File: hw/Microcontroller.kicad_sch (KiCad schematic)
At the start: 22 parts, among them SW1 Reset, SW2 Boot0, U3 STM32G431CBT6, Y1 16 MHz

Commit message: huge schematic rework
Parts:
- D1, D2: footprint Resistor_SMD:R_0603_1608Metric -> LED_THT:LED_D5.0mm
- R5, R6: value 470 -> 1k; LCSC C23179 -> C21190
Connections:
- net +3.3V: now also SW2.2; no longer R4.2
- net GND: now also R4.1; no longer SW2.1
- net STM_BOOT0: now also R4.2; no longer R4.1
- net at R3.1: now also SW2.1; no longer SW2.2
- net STM_USART1_RX: no longer names the net of U3.32 (PA10)
- no-connect marks 16 -> 17
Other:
- moved on the sheet: C17, C18, R1, R2, R3, R4, SW1, SW2

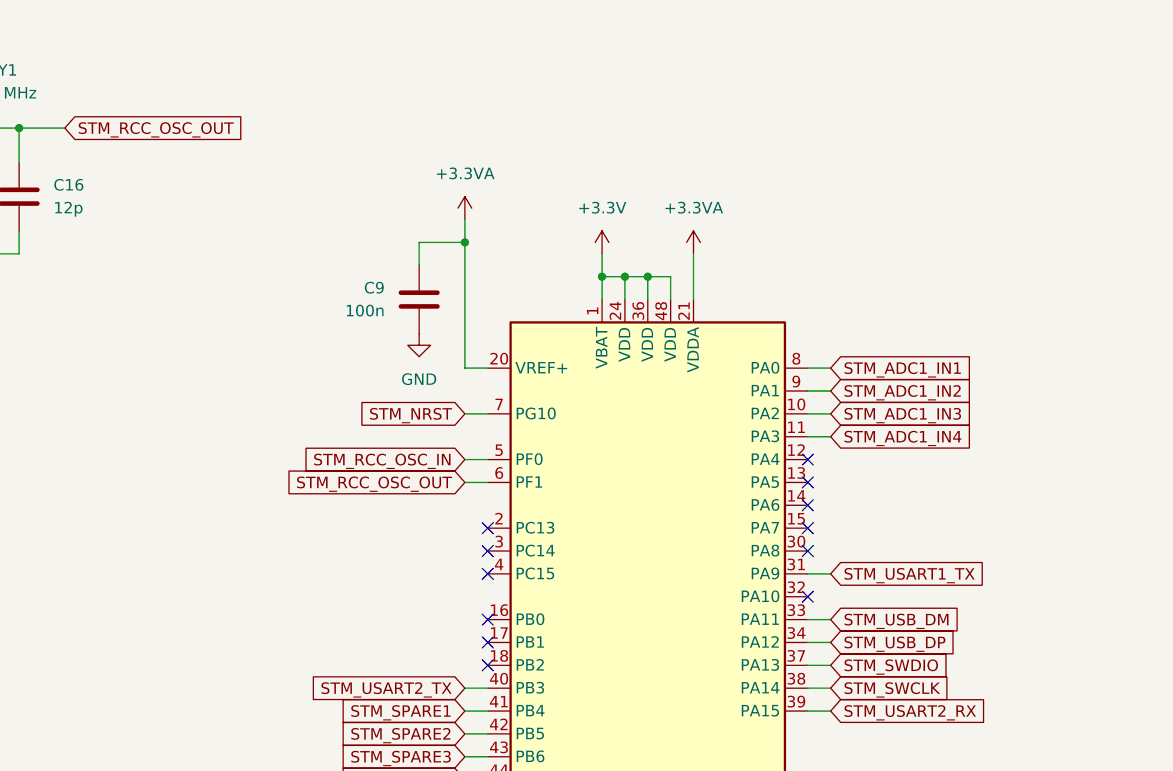
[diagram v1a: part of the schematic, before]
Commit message: added new pcb design, ERC errors not fixed yet
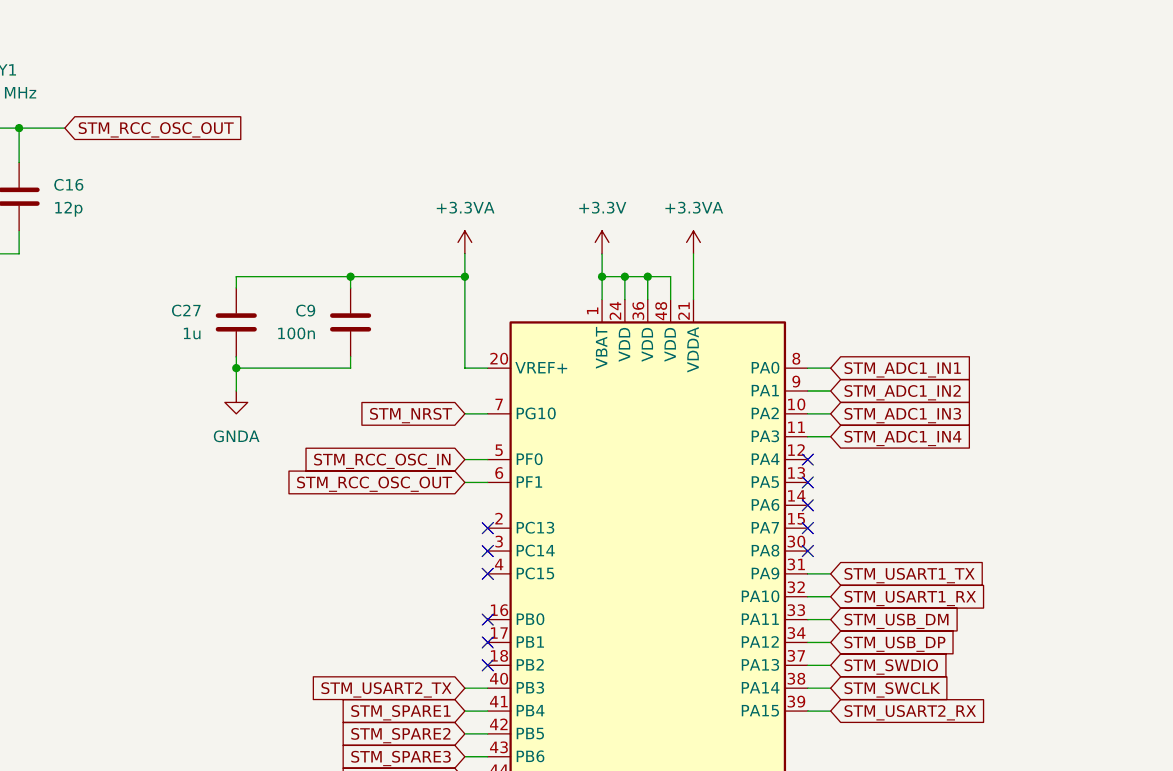
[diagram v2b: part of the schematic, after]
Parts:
- added C27: 1u, Capacitor_SMD:C_0603_1608Metric, symbol Device:C
- D1, D2: footprint LED_THT:LED_D5.0mm -> LED_THT:LED_D3.0mm
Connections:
- net +3.3VA: now also C27.1
- net GND: no longer C9.2
- net GNDA: now also C9.2, C27.2
- net STM_USART1_RX: now reaches U3.32 (PA10)
- no-connect marks 17 -> 16
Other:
- moved on the sheet: C9

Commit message: updates to hardware layer
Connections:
- net STM_ADC2_IN17: now reaches U3.12 (PA4)
- net STM_ADC2_IN13: now reaches U3.13 (PA5)
- net STM_ADC2_IN3: now reaches U3.14 (PA6)
- net STM_ADC2_IN4: now reaches U3.15 (PA7)
- no-connect marks 16 -> 12
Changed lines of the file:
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@@
 	)
 	(no_connect
-		(at 161.29 83.82)
+		(at 125.73 127)
+	)
+	(no_connect
+		(at 125.73 137.16)
+	)
+	(no_connect
+		(at 125.73 134.62)
+	)
+	(no_connect
+		(at 125.73 93.98)
 	)
 	(no_connect
@@
 	)
 	(no_connect
-		(at 125.73 127)
-	)
-	(no_connect
-		(at 125.73 137.16)
-	)
-	(no_connect
-		(at 125.73 134.62)
-	)
-	(no_connect
-		(at 125.73 93.98)
-	)
-	(no_connect
-		(at 161.29 86.36)
-	)
-	(no_connect
 		(at 125.73 88.9)
-	)
-	(no_connect
-		(at 161.29 88.9)
 	)
 	(no_connect
@@
 	)
 	(no_connect
-		(at 161.29 81.28)
-	)
-	(no_connect
 		(at 125.73 101.6)
 	)
@@
 	(wire
 		(pts
+			(xy 161.29 83.82) (xy 163.83 83.82)
+		)
+		(stroke
+			(width 0)
+			(type default)
+		)
+	)
+	(wire
+		(pts
 			(xy 123.19 114.3) (xy 125.73 114.3)
 		)
@@
 	(wire
 		(pts
+			(xy 161.29 81.28) (xy 163.83 81.28)
+		)
+		(stroke
+			(width 0)
+			(type default)
+		)
+	)
+	(wire
+		(pts
 			(xy 43.18 148.59) (xy 43.18 151.13)
 		)
@@
 	(wire
 		(pts
+			(xy 161.29 86.36) (xy 163.83 86.36)
+		)
+		(stroke
+			(width 0)
+			(type default)
+		)
+	)
+	(wire
+		(pts
 			(xy 148.59 147.32) (xy 146.05 147.32)
 		)
@@
 	(wire
 		(pts
+			(xy 161.29 88.9) (xy 163.83 88.9)
+		)
+		(stroke
+			(width 0)
+			(type default)
+		)
+	)
+	(wire
+		(pts
 			(xy 205.74 27.94) (xy 218.44 27.94)
 		)
@@
 		)
 	)
+	(global_label "STM_ADC2_IN17"
+		(shape input)
+		(at 163.83 81.28 0)
+		(fields_autoplaced yes)
+		(effects
+			(font
+				(size 1.27 1.27)
+			)
+			(justify left)
+		)
+		(property "Intersheetrefs" "${INTERSHEET_REFS}"
+			(at 181.5713 81.28 0)
+			(effects
+				(font
+					(size 1.27 1.27)
+				)
+				(justify left)
+				(hide yes)
+			)
+		)
+	)
 	(global_label "STM_SPARE3"
 		(shape input)
@@
 		)
 	)
+	(global_label "STM_ADC2_IN13"
+		(shape input)
+		(at 163.83 83.82 0)
+		(fields_autoplaced yes)
+		(effects
+			(font
+				(size 1.27 1.27)
+			)
+			(justify left)
+		)
+		(property "Intersheetrefs" "${INTERSHEET_REFS}"
+			(at 181.5713 83.82 0)
+			(effects
+				(font
+					(size 1.27 1.27)
+				)
+				(justify left)
+				(hide yes)
+			)
+		)
+	)
 	(global_label "STM_LED2"
 		(shape input)
@@
 		)
 	)
+	(global_label "STM_ADC2_IN3"
+		(shape input)
+		(at 163.83 86.36 0)
+		(fields_autoplaced yes)
+		(effects
+			(font
+				(size 1.27 1.27)
+			)
+			(justify left)
+		)
+		(property "Intersheetrefs" "${INTERSHEET_REFS}"
+			(at 180.3618 86.36 0)
+			(effects
+				(font
+					(size 1.27 1.27)
+				)
+				(justify left)
+				(hide yes)
+			)
+		)
+	)
 	(global_label "STM_SWCLK"
 		(shape input)
@@
 			(effects
 				(font
+					(size 1.27 1.27)
+				)
+				(justify left)
+				(hide yes)
+			)
+		)
+	)
+	(global_label "STM_ADC2_IN4"
+		(shape input)
+		(at 163.83 88.9 0)
+		(fields_autoplaced yes)
+		(effects
+			(font
+				(size 1.27 1.27)
+			)
+			(justify left)
+		)
+		(property "Intersheetrefs" "${INTERSHEET_REFS}"
+			(at 180.3618 88.9 0)
+			(effects
+				(font

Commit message: removed MIDI Thru and updated Connector positioning
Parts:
- D1, D2: footprint LED_THT:LED_D3.0mm -> LED_THT:LED_D5.0mm
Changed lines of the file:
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@@
 			)
 		)
-		(property "Footprint" "LED_THT:LED_D3.0mm"
+		(property "Footprint" "LED_THT:LED_D5.0mm"
 			(at 55.88 154.94 0)
 			(effects
@@
 			)
 		)
-		(property "Footprint" "LED_THT:LED_D3.0mm"
+		(property "Footprint" "LED_THT:LED_D5.0mm"
 			(at 43.18 154.94 0)
 			(effects

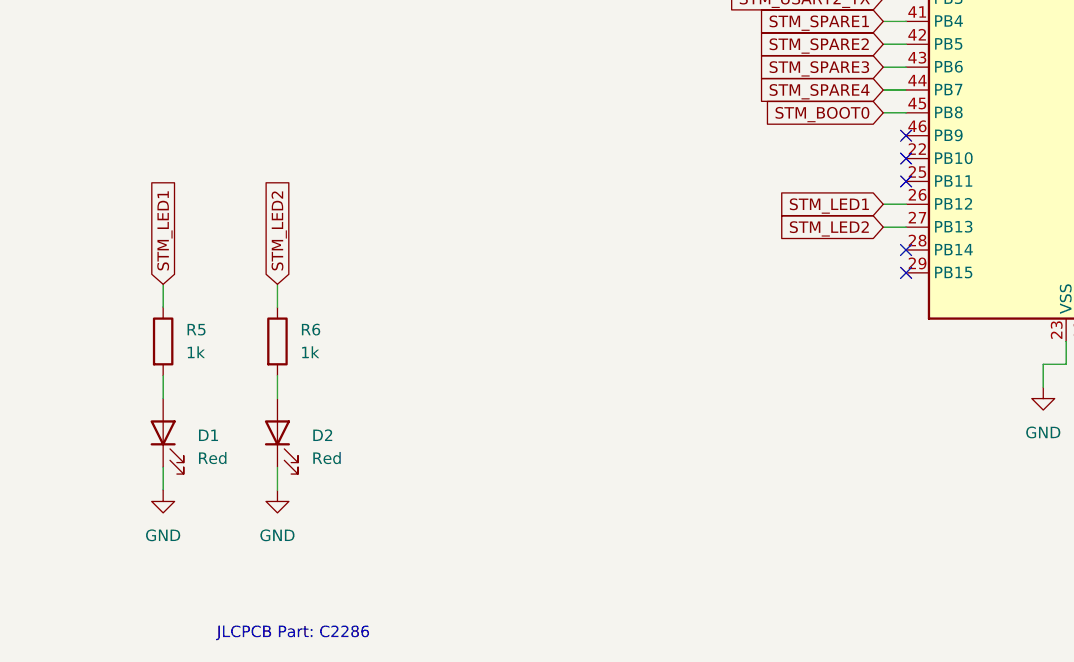
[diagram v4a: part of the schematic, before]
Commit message: updated connector positions and added new RGB led
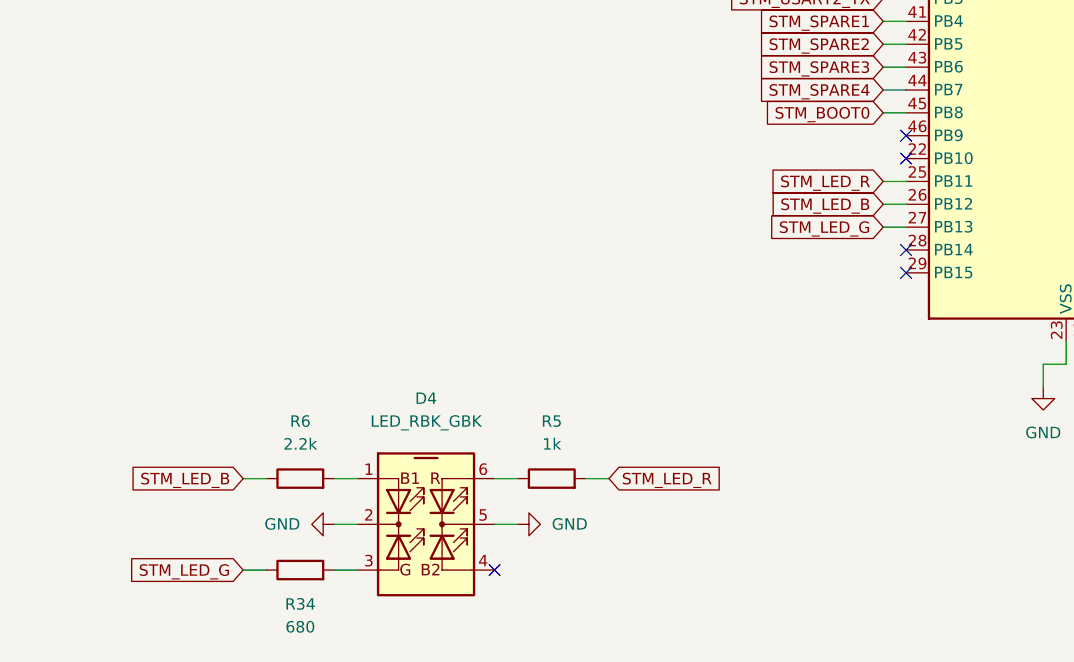
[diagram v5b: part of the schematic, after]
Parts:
- removed D1, D2: Red, LED_THT:LED_D5.0mm, symbol Device:LED
- added D4: LED_RBK_GBK, LED_THT_6Pin:LED_D5.0mm_6Pin, symbol Midi_Expressor:LED_RBK_GBK
- added R34: 680, Resistor_SMD:R_0603_1608Metric, symbol Device:R
- R6: value 1k -> 2.2k; LCSC C21190 -> (none)
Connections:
- net GND: now also D4.2 (K1), D4.5 (K2)
- net at R6.2: now also D4.1 (B1A)
- net STM_LED_R: now reaches U3.25 (PB11)
- net STM_LED_R: now also R5.2
- net STM_LED1: no longer names the net of R5.1
- net STM_LED1: now also D4.6 (RA); no longer U3.26 (PB12)
- net STM_LED2 renamed STM_LED_B
- net STM_LED_B: now also U3.26 (PB12); no longer U3.27 (PB13)
- new net: D4.3 (GA), R34.2
- new net STM_LED_G: R34.1, U3.27 (PB13)
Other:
- note removed: "JLCPCB Part: C2286"
- moved on the sheet: R5

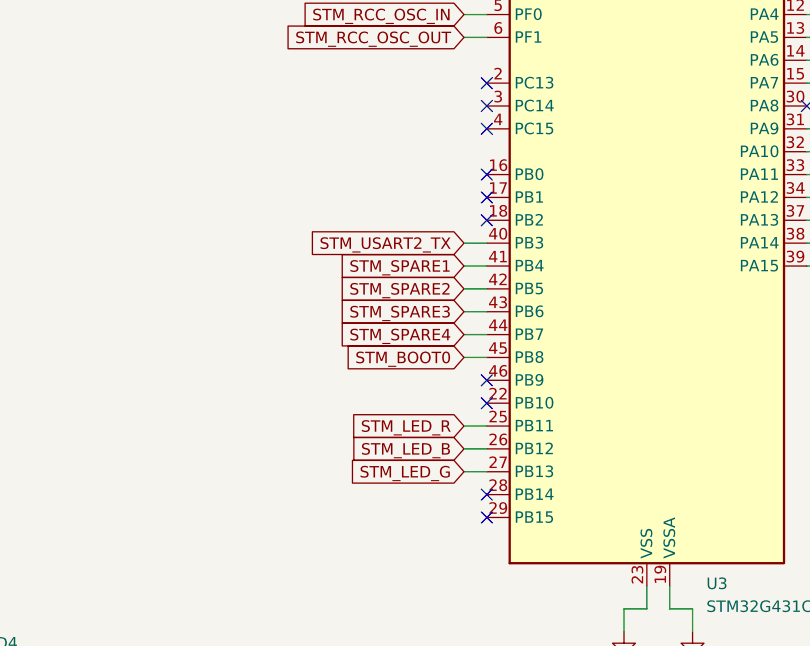
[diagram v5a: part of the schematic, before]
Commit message: added new LED traces to hardware
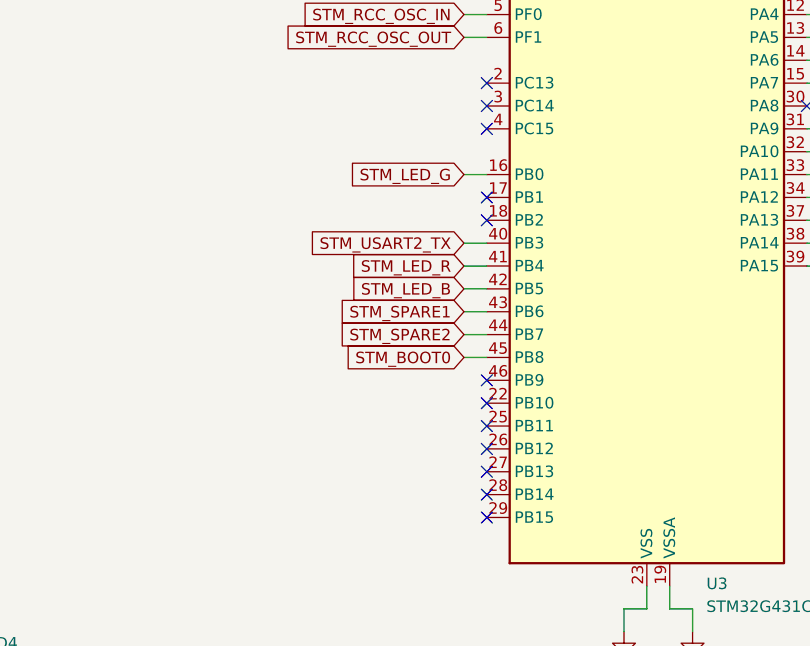
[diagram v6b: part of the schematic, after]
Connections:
- net STM_SPARE3 is gone; now on net STM_SPARE1: U3.43 (PB6)
- net STM_SPARE4 is gone; now on net STM_SPARE2: U3.44 (PB7)
- net STM_LED_B: now also U3.42 (PB5); no longer U3.26 (PB12)
- net STM_LED_G: now also U3.16 (PB0); no longer U3.27 (PB13)
- net STM_LED_R: now also U3.41 (PB4); no longer U3.25 (PB11)
- net STM_SPARE1: no longer U3.41 (PB4)
- net STM_SPARE2: no longer U3.42 (PB5)
- no-connect marks 12 -> 14

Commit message: added final production files for version 2
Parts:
- R34: LCSC (none) -> C23228
- R6: LCSC (none) -> C4190
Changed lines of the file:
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@@
+			)
+		)
+		(property "LCSC" "C4190"
+			(at 58.42 153.67 0)
+			(effects
+				(font
+					(size 1.27 1.27)
+				)
+				(hide yes)
 			)
 		)
@@
 			(effects
 				(font
+					(size 1.27 1.27)
+				)
+				(hide yes)
+			)
+		)
+		(property "LCSC" "C23228"
+			(at 58.42 173.99 0)
+			(effects
+				(font
